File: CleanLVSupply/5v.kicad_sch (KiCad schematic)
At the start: 19 parts, among them U5 LMR54406F, U6 TPS7A47

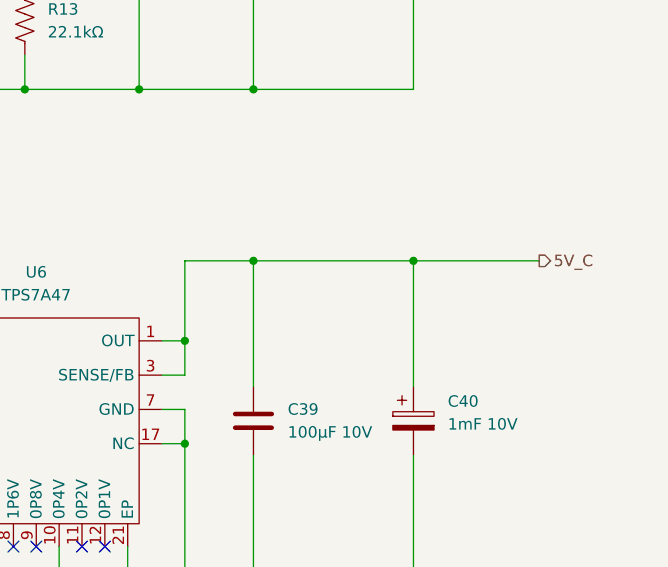
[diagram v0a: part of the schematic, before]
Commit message: HiFiDAC routing done, CleanLVSupply fuses added
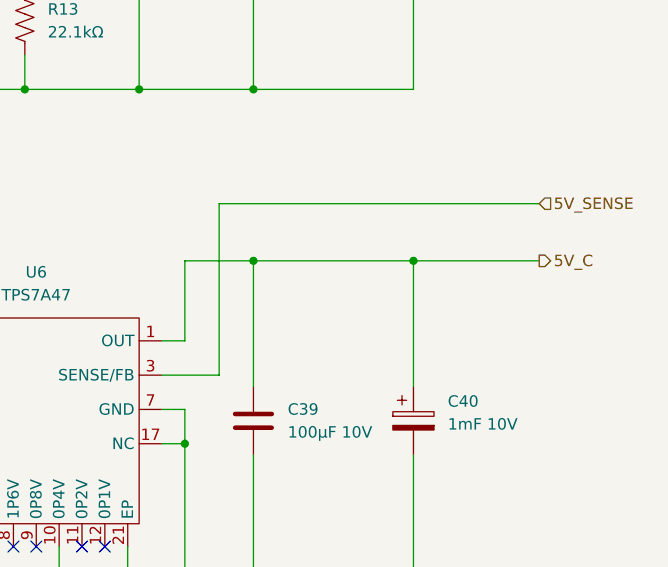
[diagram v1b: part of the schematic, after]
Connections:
- net 5V_C: no longer U6.3 (SENSE/FB)
- new net 5V_SENSE: U6.3 (SENSE/FB)
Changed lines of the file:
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@@
-	)
-	(junction
-		(at 175.26 115.57)
-		(diameter 0)
-		(color 0 0 0 0)
 	)
 	(junction
@@
 	(wire
 		(pts
+			(xy 179.07 100.33) (xy 214.63 100.33)
+		)
+		(stroke
+			(width 0)
+			(type default)
+		)
+	)
+	(wire
+		(pts
 			(xy 132.08 135.89) (xy 132.08 142.24)
 		)
@@
 	(wire
 		(pts
-			(xy 175.26 119.38) (xy 175.26 115.57)
-		)
-		(stroke
-			(width 0)
-			(type default)
-		)
-	)
-	(wire
-		(pts
 			(xy 157.48 71.12) (xy 157.48 76.2)
 		)
@@
 	(wire
 		(pts
+			(xy 179.07 119.38) (xy 179.07 100.33)
+		)
+		(stroke
+			(width 0)
+			(type default)
+		)
+	)
+	(wire
+		(pts
 			(xy 144.78 119.38) (xy 142.24 119.38)
 		)
@@
 	(wire
 		(pts
-			(xy 172.72 119.38) (xy 175.26 119.38)
+			(xy 172.72 119.38) (xy 179.07 119.38)
 		)
 		(stroke
@@
 		)
 	)
+	(hierarchical_label "5V_SENSE"
+		(shape input)
+		(at 214.63 100.33 0)
+		(fields_autoplaced yes)
+		(effects
+			(font
+				(size 1.27 1.27)
+			)
+			(justify left)
+		)
+	)
